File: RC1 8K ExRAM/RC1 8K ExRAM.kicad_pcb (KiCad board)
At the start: 2 copper layers, 99.1 x 83.8 mm, 32 parts, among them J1 Expansion, J2 ADDRESS, U1 74LS138, U2 74LS00, U3 74HC595, U4 74HC595, U5 HM62256BLP-7, U6 74LS244, U7 74LS244, U8 74LS245

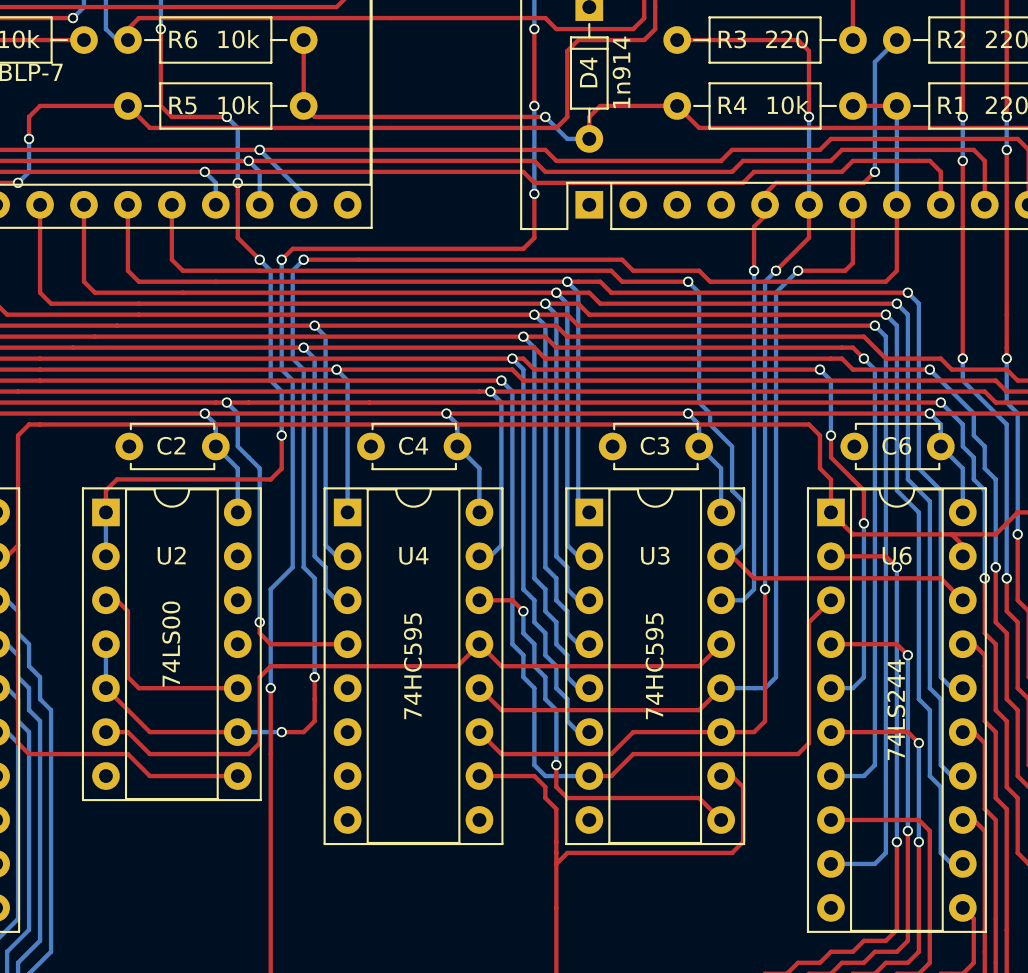
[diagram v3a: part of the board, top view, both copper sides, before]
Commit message: Tweak ExRAM signalling
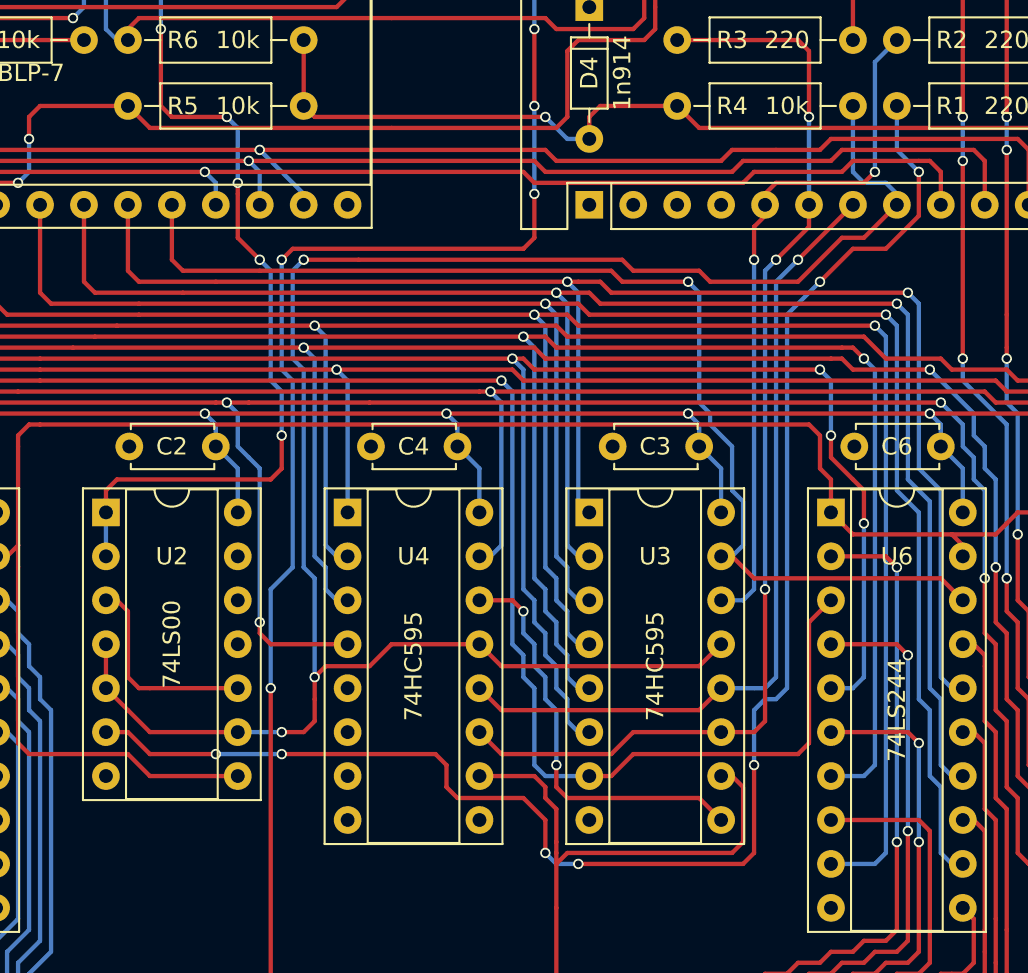
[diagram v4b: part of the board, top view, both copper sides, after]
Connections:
- net ~EXT_CS renamed ~RC1_CS
- A1 pad 8: BUS_EN -> CONTROL
- R1 pad 2: BUS_EN -> BUSY
- R4 pad 1: BUS_EN -> CONTROL
- U2 pad 4: BUS_EN -> CONTROL
- U2 pad 5: BUS_EN -> CONTROL
- U2 pad 6: ~BUS_EN -> BUSY
- U2 pad 9: BUS_EN -> CONTROL
- U3 pad 13: ~BUS_EN -> CONTROL
- U4 pad 13: ~BUS_EN -> CONTROL
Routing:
- net CONTROL: track 0.00 -> 112.9 mm, vias 0 -> 3
- net BUSY: track 0.00 -> 91.9 mm, vias 0 -> 7
- net BUS_EN: track 90.5 -> 0.00 mm, vias 3 -> 0
- net ~BUS_EN: track 42.0 -> 0.00 mm
- net SHIFT_LATCH: track 49.8 -> 48.2 mm
- net SHIFT_CLK: track 66.8 -> 66.1 mm

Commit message: ExRAM silkscreen updated
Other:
- board text added: "(A0-A7)"
- board text added: "(A8-A12)"
- board text added: "ADDRESS BUFFER"
- board text added: "ADDRESS DECODING"
- board text added: "ADDRESS SHIFT REGISTER"
- board text added: "Arduino Nano v3.x"
- board text added: "CONTROL LOGIC"
- board text added: "DATA IN/OUT"
- board text added: "STATIC RAM"
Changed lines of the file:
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@@
     (area 95.174999 64.694999 194.385001 148.665001)
     (thickness 1.6)
-    (drawings 140)
+    (drawings 207)
     (tracks 1823)
     (zones 0)
@@
     )
   )
+  (gr_text "Arduino\nNano v3.x" (at 189.23 83.82) (layer B.SilkS)
+    (effects (font (size 0.8 0.8) (thickness 0.1)) (justify mirror))
+  )
+  (gr_text "STATIC\nRAM" (at 139.7 83.82) (layer B.SilkS)
+    (effects (font (size 0.8 0.8) (thickness 0.1)) (justify mirror))
+  )
+  (gr_text "ADDRESS\nDECODING" (at 102.87 119.38) (layer B.SilkS)
+    (effects (font (size 0.8 0.8) (thickness 0.1)) (justify mirror))
+  )
+  (gr_text "DATA\nIN/OUT" (at 116.84 119.38) (layer B.SilkS)
+    (effects (font (size 0.8 0.8) (thickness 0.1)) (justify mirror))
+  )
+  (gr_text "(A8-A12)" (at 186.69 125.095) (layer B.SilkS)
+    (effects (font (size 0.8 0.8) (thickness 0.1)) (justify mirror))
+  )
+  (gr_text "(A0-A7)" (at 172.72 125.095) (layer B.SilkS)
+    (effects (font (size 0.8 0.8) (thickness 0.1)) (justify mirror))
+  )
+  (gr_text "(A8-A12)" (at 144.78 125.095) (layer B.SilkS)
+    (effects (font (size 0.8 0.8) (thickness 0.1)) (justify mirror))
+  )
+  (gr_text "(A0-A7)" (at 158.75 125.095) (layer B.SilkS)
+    (effects (font (size 0.8 0.8) (thickness 0.1)) (justify mirror))
+  )
+  (gr_text "ADDRESS\nBUFFER" (at 186.69 119.38) (layer B.SilkS)
+    (effects (font (size 0.8 0.8) (thickness 0.1)) (justify mirror))
+  )
+  (gr_text "ADDRESS\nBUFFER" (at 172.72 119.38) (layer B.SilkS)
+    (effects (font (size 0.8 0.8) (thickness 0.1)) (justify mirror))
+  )
+  (gr_text "ADDRESS\nSHIFT\nREGISTER" (at 158.75 120.015) (layer B.SilkS)
+    (effects (font (size 0.8 0.8) (thickness 0.1)) (justify mirror))
+  )
+  (gr_text "ADDRESS\nSHIFT\nREGISTER" (at 144.78 120.015) (layer B.SilkS)
+    (effects (font (size 0.8 0.8) (thickness 0.1)) (justify mirror))
+  )
+  (gr_text "CONTROL\nLOGIC" (at 130.81 119.38) (layer B.SilkS)
+    (effects (font (size 0.8 0.8) (thickness 0.1)) (justify mirror))
+  )
+  (gr_line (start 193.675 95.885) (end 191.135 95.885) (angle 90) (layer B.SilkS) (width 0.2))
+  (gr_line (start 193.675 80.645) (end 193.675 95.885) (angle 90) (layer B.SilkS) (width 0.2))
+  (gr_line (start 191.135 80.645) (end 193.675 80.645) (angle 90) (layer B.SilkS) (width 0.2))
+  (gr_line (start 150.495 95.885) (end 154.305 95.885) (angle 90) (layer B.SilkS) (width 0.2))
+  (gr_line (start 150.495 80.645) (end 150.495 95.885) (angle 90) (layer B.SilkS) (width 0.2))
+  (gr_line (start 154.305 80.645) (end 150.495 80.645) (angle 90) (layer B.SilkS) (width 0.2))
+  (gr_line (start 142.875 95.885) (end 141.605 95.885) (angle 90) (layer B.SilkS) (width 0.2))
+  (gr_line (start 142.875 80.645) (end 142.875 95.885) (angle 90) (layer B.SilkS) (width 0.2))
+  (gr_line (start 141.605 80.645) (end 142.875 80.645) (angle 90) (layer B.SilkS) (width 0.2))
+  (gr_line (start 106.045 80.645) (end 107.315 80.645) (angle 90) (layer B.SilkS) (width 0.2))
+  (gr_line (start 106.045 95.885) (end 106.045 80.645) (angle 90) (layer B.SilkS) (width 0.2))
+  (gr_line (start 107.315 95.885) (end 106.045 95.885) (angle 90) (layer B.SilkS) (width 0.2))
+  (gr_line (start 190.5 138.43) (end 190.5 137.16) (angle 90) (layer B.SilkS) (width 0.2))
+  (gr_line (start 182.88 138.43) (end 190.5 138.43) (angle 90) (layer B.SilkS) (width 0.2))
+  (gr_line (start 182.88 137.16) (end 182.88 138.43) (angle 90) (layer B.SilkS) (width 0.2))
+  (gr_line (start 176.53 138.43) (end 176.53 137.16) (angle 90) (layer B.SilkS) (width 0.2))
+  (gr_line (start 168.91 138.43) (end 176.53 138.43) (angle 90) (layer B.SilkS) (width 0.2))
+  (gr_line (start 168.91 137.16) (end 168.91 138.43) (angle 90) (layer B.SilkS) (width 0.2))
+  (gr_line (start 162.56 133.35) (end 162.56 132.08) (angle 90) (layer B.SilkS) (width 0.2))
+  (gr_line (start 154.94 133.35) (end 162.56 133.35) (angle 90) (layer B.SilkS) (width 0.2))
+  (gr_line (start 154.94 132.08) (end 154.94 133.35) (angle 90) (layer B.SilkS) (width 0.2))
+  (gr_line (start 148.59 133.35) (end 148.59 132.08) (angle 90) (layer B.SilkS) (width 0.2))
+  (gr_line (start 140.97 133.35) (end 148.59 133.35) (angle 90) (layer B.SilkS) (width 0.2))
+  (gr_line (start 140.97 132.08) (end 140.97 133.35) (angle 90) (layer B.SilkS) (width 0.2))
+  (gr_line (start 134.62 130.81) (end 134.62 129.54) (angle 90) (layer B.SilkS) (width 0.2))
+  (gr_line (start 127 130.81) (end 134.62 130.81) (angle 90) (layer B.SilkS) (width 0.2))
+  (gr_line (start 127 129.54) (end 127 130.81) (angle 90) (layer B.SilkS) (width 0.2))
+  (gr_line (start 120.65 138.43) (end 120.65 137.16) (angle 90) (layer B.SilkS) (width 0.2))
+  (gr_line (start 113.03 138.43) (end 120.65 138.43) (angle 90) (layer B.SilkS) (width 0.2))
+  (gr_line (start 113.03 137.16) (end 113.03 138.43) (angle 90) (layer B.SilkS) (width 0.2))
+  (gr_line (start 106.68 133.35) (end 106.68 132.08) (angle 90) (layer B.SilkS) (width 0.2))
+  (gr_line (start 99.06 133.35) (end 106.68 133.35) (angle 90) (layer B.SilkS) (width 0.2))
+  (gr_line (start 99.06 132.08) (end 99.06 133.35) (angle 90) (layer B.SilkS) (width 0.2))
+  (gr_line (start 190.5 111.76) (end 190.5 113.03) (angle 90) (layer B.SilkS) (width 0.2))
+  (gr_line (start 182.88 111.76) (end 190.5 111.76) (angle 90) (layer B.SilkS) (width 0.2))
+  (gr_line (start 182.88 113.03) (end 182.88 111.76) (angle 90) (layer B.SilkS) (width 0.2))
+  (gr_line (start 176.53 111.76) (end 176.53 113.03) (angle 90) (layer B.SilkS) (width 0.2))
+  (gr_line (start 168.91 111.76) (end 176.53 111.76) (angle 90) (layer B.SilkS) (width 0.2))
+  (gr_line (start 168.91 113.03) (end 168.91 111.76) (angle 90) (layer B.SilkS) (width 0.2))
+  (gr_line (start 162.56 111.76) (end 162.56 113.03) (angle 90) (layer B.SilkS) (width 0.2))
+  (gr_line (start 154.94 111.76) (end 162.56 111.76) (angle 90) (layer B.SilkS) (width 0.2))
+  (gr_line (start 154.94 113.03) (end 154.94 111.76) (angle 90) (layer B.SilkS) (width 0.2))
+  (gr_line (start 148.59 111.76) (end 148.59 113.03) (angle 90) (layer B.SilkS) (width 0.2))
+  (gr_line (start 140.97 111.76) (end 148.59 111.76) (angle 90) (layer B.SilkS) (width 0.2))
+  (gr_line (start 140.97 113.03) (end 140.97 111.76) (angle 90) (layer B.SilkS) (width 0.2))
+  (gr_line (start 134.62 111.76) (end 134.62 113.03) (angle 90) (layer B.SilkS) (width 0.2))
+  (gr_line (start 127 111.76) (end 134.62 111.76) (angle 90) (layer B.SilkS) (width 0.2))
+  (gr_line (start 127 113.03) (end 127 111.76) (angle 90) (layer B.SilkS) (width 0.2))
+  (gr_line (start 120.65 111.76) (end 120.65 113.03) (angle 90) (layer B.SilkS) (width 0.2))
+  (gr_line (start 113.03 111.76) (end 120.65 111.76) (angle 90) (layer B.SilkS) (width 0.2))
+  (gr_line (start 113.03 113.03) (end 113.03 111.76) (angle 90) (layer B.SilkS) (width 0.2))
+  (gr_line (start 106.68 111.76) (end 106.68 113.03) (angle 90) (layer B.SilkS) (width 0.2))
+  (gr_line (start 99.06 111.76) (end 106.68 111.76) (angle 90) (layer B.SilkS) (width 0.2))
+  (gr_line (start 99.06 113.03) (end 99.06 111.76) (angle 90) (layer B.SilkS) (width 0.2))
   (gr_text "Revision B" (at 95.885 145.415) (layer B.SilkS)
     (effects (font (size 1 1) (thickness 0.15)) (justify right mirror))

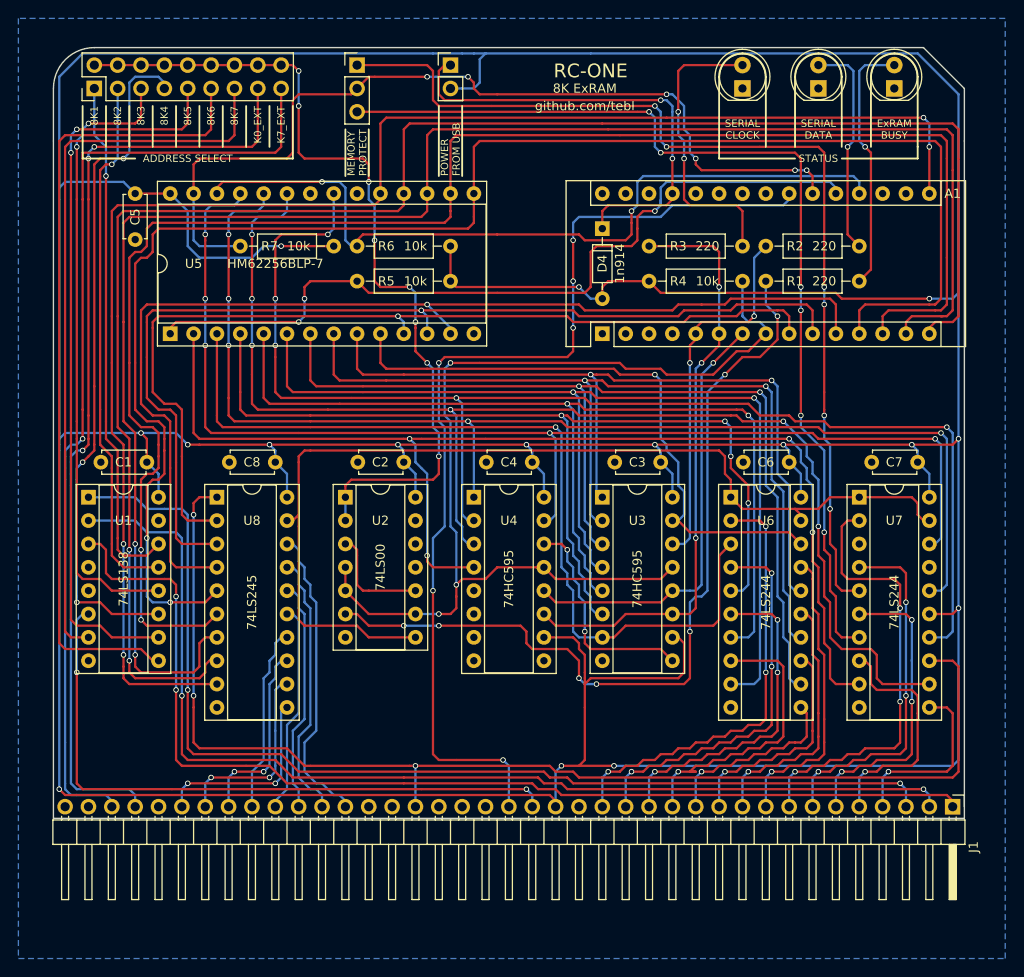
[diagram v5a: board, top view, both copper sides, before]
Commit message: Attempted ExRAM memory backup
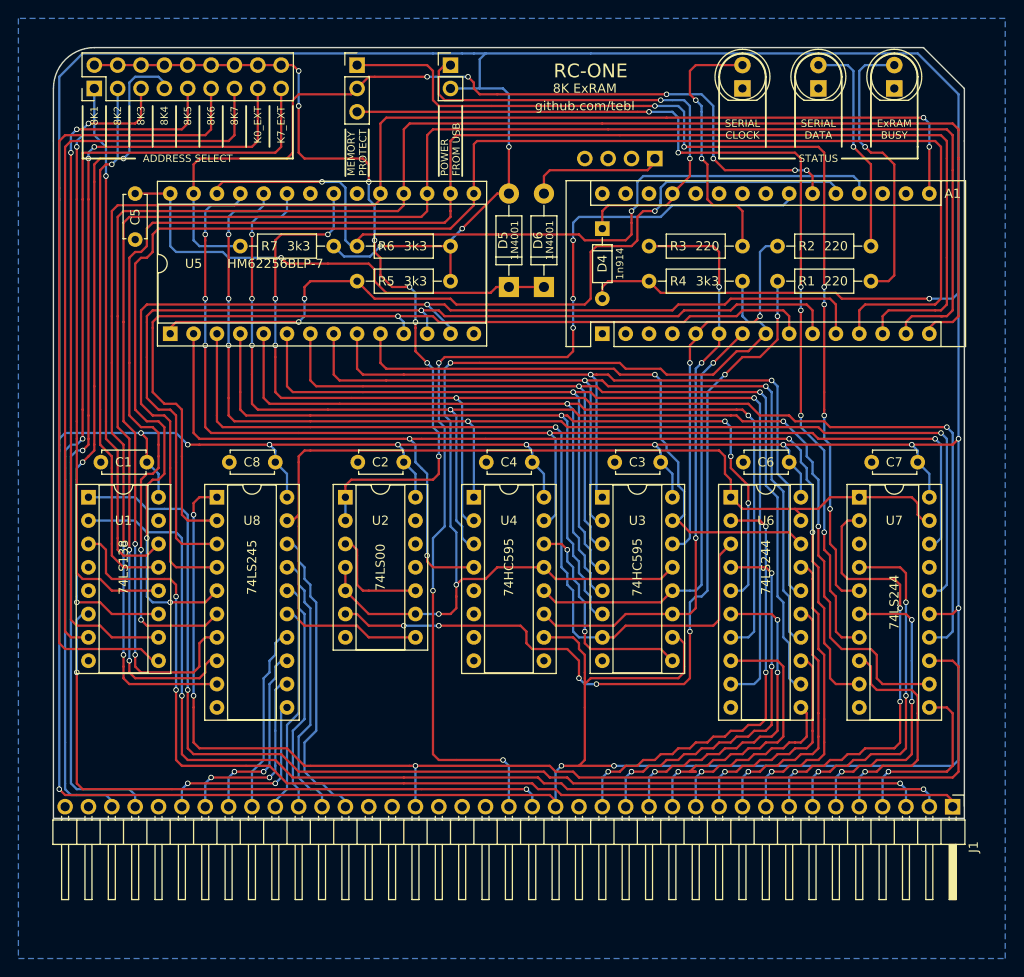
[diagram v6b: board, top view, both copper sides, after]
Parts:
- added D5: 1N4001, Diodes_THT:D_DO-41_SOD81_P10.16mm_Horizontal, F.Cu at (144.8, 90.8)
- added D6: 1N4001, Diodes_THT:D_DO-41_SOD81_P10.16mm_Horizontal, F.Cu at (148.6, 90.8)
- added J3: BATTERY, Pin_Headers:Pin_Header_Angled_1x04_Pitch2.54mm, B.Cu at (160.7, 76.8)
- R4, R5, R6, R7: value 10k -> 3k3
- moved R1 1.27 mm to (184.2, 90.2)
- moved R2 1.27 mm to (184.2, 86.4)
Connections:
- C5 pad 1: VCC -> /SRAM_VCC
- U5 pad 28: VCC -> /SRAM_VCC
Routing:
- net /SRAM_VCC: track 0.00 -> 53.3 mm, vias 0 -> 1
- net VCC: track 643.1 -> 626.8 mm, vias 16 -> 17
- net /BATTERY: track 0.00 -> 15.0 mm
- net Net-(D1-Pad2): track 28.0 -> 31.4 mm
- net Net-(D3-Pad2): track 32.2 -> 28.9 mm
- net Net-(A1-Pad27): track 50.2 -> 52.9 mm
- net /EX_A14: track 89.5 -> 91.3 mm
- net SHIFT_DATA: track 41.6 -> 42.9 mm
- net /EX_D3: track 175.7 -> 174.7 mm
- net Net-(J2-Pad10): track 92.7 -> 91.9 mm
- net BUSY: track 91.9 -> 91.4 mm
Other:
- board text added: "+"
- board text added: "-"
- board text added: "Revision C"
- board text removed: "Revision B"

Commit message: Separate SRAM CS control
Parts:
- added R8: 3k3, Resistors_THT:R_Axial_DIN0207_L6.3mm_D2.5mm_P10.16mm_Horizontal, F.Cu at (125.7, 90.2)
- D4: value 1n914 -> 1N4001
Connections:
- A1 pad 24: (no net) -> /EX_~CS
- C5 pad 1: /SRAM_VCC -> VMEM
- D5 pad 1: /SRAM_VCC -> VMEM
- D6 pad 1: /SRAM_VCC -> VMEM
- R7 pad 2: VCC -> VMEM
- U5 pad 20: GND -> /EX_~CS
- U5 pad 28: /SRAM_VCC -> VMEM
- U7 pad 17: GND -> ~RC1_CS
- U7 pad 3: (no net) -> /EX_~CS
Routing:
- net /EX_~CS: track 0.00 -> 114.2 mm, vias 0 -> 7
- net VMEM: track 0.00 -> 58.2 mm, vias 0 -> 1
- net /SRAM_VCC: track 53.3 -> 0.00 mm, vias 1 -> 0
- net VCC: track 626.8 -> 613.2 mm, vias 17 -> 16
- net ~RC1_CS: track 110.4 -> 117.0 mm
- net /EX_A14: track 91.3 -> 90.3 mm
- net /RESET: track 110.8 -> 110.1 mm, vias 6 -> 4
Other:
- board text added: "Revision D"
- board text removed: "Revision C"
